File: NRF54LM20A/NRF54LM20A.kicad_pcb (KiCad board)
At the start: 4 copper layers, 10.8 x 22 mm, 39 parts, among them IC3 NMH1000T1, J1 Conn_ARM_SWD_TagConnect_TC203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, U1 S25HS512TFANHI010, U2 nRF54LM20A-QGAA, U3 SR4W035, U4 IM67D128BV01, U5 TXS0102DQE, Y1 CX2016DB32000D0WZRC1

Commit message: straight up routin it
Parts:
- added C25: 10u, Capacitor_SMD:C_0402_1005Metric, F.Cu at (89.5, 76.7)
- added C26: 10u, Capacitor_SMD:C_0603_1608Metric, F.Cu at (91.8, 81.0)
- added C27: 47n 25V, Capacitor_SMD:C_0402_1005Metric, F.Cu at (90.8, 82.7)
- added C28: 0.47u 25V, Capacitor_SMD:C_0402_1005Metric, F.Cu at (91.8, 82.7)
- added C29: 10n 25V, Capacitor_SMD:C_0201_0603Metric, F.Cu at (92.6, 82.8)
- added C30: 10u 16V, Capacitor_SMD:C_0603_1608Metric, F.Cu at (89.6, 82.2)
- added C31: 47n 25V, Capacitor_SMD:C_0402_1005Metric, F.Cu at (91.7, 89.0)
- added C32: 0.47u 25V, Capacitor_SMD:C_0402_1005Metric, F.Cu at (92.7, 89.0)
- added C33: 10n 25V, Capacitor_SMD:C_0201_0603Metric, F.Cu at (93.5, 88.8)
- added C34: TBD, Capacitor_SMD:C_0603_1608Metric, F.Cu at (91.7, 91.5)
- added C35: TBD, Capacitor_SMD:C_0603_1608Metric, F.Cu at (93.2, 91.5)
- added C36: TBD, Capacitor_SMD:C_0402_1005Metric, F.Cu at (90.5, 91.2)
- added C37: TBD, Capacitor_SMD:C_0402_1005Metric, F.Cu at (89.5, 91.2)
- added C38: 0.1u, Capacitor_SMD:C_0201_0603Metric, F.Cu at (93.9, 82.9)
- added C39: T527I107M006ATE070, Capacitor_Tantalum_SMD:CP_EIA-3216-12_Kemet-S, F.Cu at (89.8, 73.4)
- added C40: 0.1u, Capacitor_SMD:C_0201_0603Metric, F.Cu at (93.2, 79.5)
- added C41: 0.1u, Capacitor_SMD:C_0201_0603Metric, F.Cu at (91.4, 77.0)
- added C42: TBD, Capacitor_SMD:C_0201_0603Metric, F.Cu at (93.8, 77.2)
- added C43: TBD, Capacitor_SMD:C_0201_0603Metric, F.Cu at (93.5, 78.4)
- added IC1: TPS6285010MQDRLRQ1, Library:TPS6285010MQDRLRQ1, F.Cu at (91.6, 79.0)
- added IC2: BQ51013B, Package_DFN_QFN:Texas_VQFN-RHL-20_ThermalVias, F.Cu at (91.5, 85.8)
- added L2: 0.47u, Inductor_SMD:L_0603_1608Metric, F.Cu at (89.6, 79.2)
- added R1: 10k, Resistor_SMD:R_0201_0603Metric, F.Cu at (90.1, 88.8)
- added R2: TBD, Resistor_SMD:R_0201_0603Metric, F.Cu at (90.8, 88.8)
- added R3: TBD, Resistor_SMD:R_0201_0603Metric, F.Cu at (89.3, 88.8)
- added R4: TBD, Resistor_SMD:R_0201_0603Metric, F.Cu at (89.7, 90.0)
- added R5: 5.1k, Resistor_SMD:R_0201_0603Metric, F.Cu at (93.9, 80.0)
- added R6: 10k, Resistor_SMD:R_0201_0603Metric, F.Cu at (93.9, 81.5)
- added TP1: RCU-0C, digikey-footprints:PROBE_PAD_0603, B.Cu at (90.2, 92.0)
- added TP2: RCU-0C, digikey-footprints:PROBE_PAD_0603, B.Cu at (90.2, 90.5)
- added TP3: RCU-0C, digikey-footprints:PROBE_PAD_0603, B.Cu at (92.8, 90.5)
- added TP4: RCU-0C, digikey-footprints:PROBE_PAD_0603, B.Cu at (92.8, 92.0)
- added U6: LSM6DSV16B, Package_LGA:LGA-14_3x2.5mm_P0.5mm_LayoutBorder3x4y, F.Cu at (92.6, 74.5)
- C19: value 6TPS150MUD -> 10u; footprint Capacitor_Tantalum_SMD:CP_EIA-3528-21_Kemet-B -> Capacitor_SMD:C_0402_1005Metric
- moved C19 25.7 mm to (90.5, 76.7), turned to 90 degrees
- moved J1 19.8 mm to (92.5, 74.5), turned to 90 degrees
- moved C20 0.09 mm to (103.3, 76.6)
- moved C17 0.05 mm to (103.3, 73.7)
- moved C18 0.05 mm to (103.3, 75.2)
- moved U1 0.05 mm to (98.6, 74.3)
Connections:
- C19 pad 1: +5V -> +1V8
- C19 pad 2: unconnected-(C19-Pad2) -> GND
- U2 pad 13: unconnected-(U2C-P1.03-Pad13) -> /Peripherals/IMU_CS
- U2 pad 14: unconnected-(U2C-P1.04-Pad14) -> /Peripherals/IMU_INT0
- U2 pad 15: unconnected-(U2C-P1.05-Pad15) -> /Peripherals/5V_SENSE
- U2 pad 16: unconnected-(U2C-P1.06-Pad16) -> /Peripherals/5V_SENSE
- U2 pad 22: unconnected-(U2C-P1.07-Pad22) -> /Peripherals/IMU_SCK
- U2 pad 23: unconnected-(U2C-P1.08-Pad23) -> /Peripherals/IMU_INT1
- U2 pad 24: unconnected-(U2C-P1.09-Pad24) -> /Peripherals/IMU_SDI
- U2 pad 25: unconnected-(U2B-P0.03-Pad25) -> /Peripherals/IMU_SDO
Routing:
- net +5V: track 5.54 -> 36.3 mm, vias 2 -> 6
- net GND: track 33.1 -> 63.3 mm, vias 17 -> 25
- net /Peripherals/IMU_SDO: track 0.00 -> 20.8 mm, vias 0 -> 3
- net /Power/AC1: track 0.00 -> 19.7 mm, vias 0 -> 3
- net /SWCLK: track 0.50 -> 20.2 mm
- net /Peripherals/IMU_SDI: track 0.00 -> 19.6 mm, vias 0 -> 3
- net NFC2: track 1.26 -> 20.0 mm, vias 1 -> 3
- net /SWDIO: track 0.71 -> 19.2 mm
- net NFC1: track 1.09 -> 18.6 mm, vias 1 -> 3
- net /Peripherals/IMU_SCK: track 0.00 -> 16.6 mm, vias 0 -> 3
- net /~{RESET}: track 0.50 -> 15.8 mm
- net /Peripherals/IMU_INT1: track 0.00 -> 15.2 mm, vias 0 -> 3
- net /Power/AC2: track 0.00 -> 11.3 mm, vias 0 -> 6
- net Net-(IC2-RECT): track 0.00 -> 11.1 mm, vias 0 -> 3
- net +1V8: track 18.7 -> 28.9 mm, vias 10 -> 14
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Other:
- board size 10.8 x 22 mm -> 15 x 22 mm

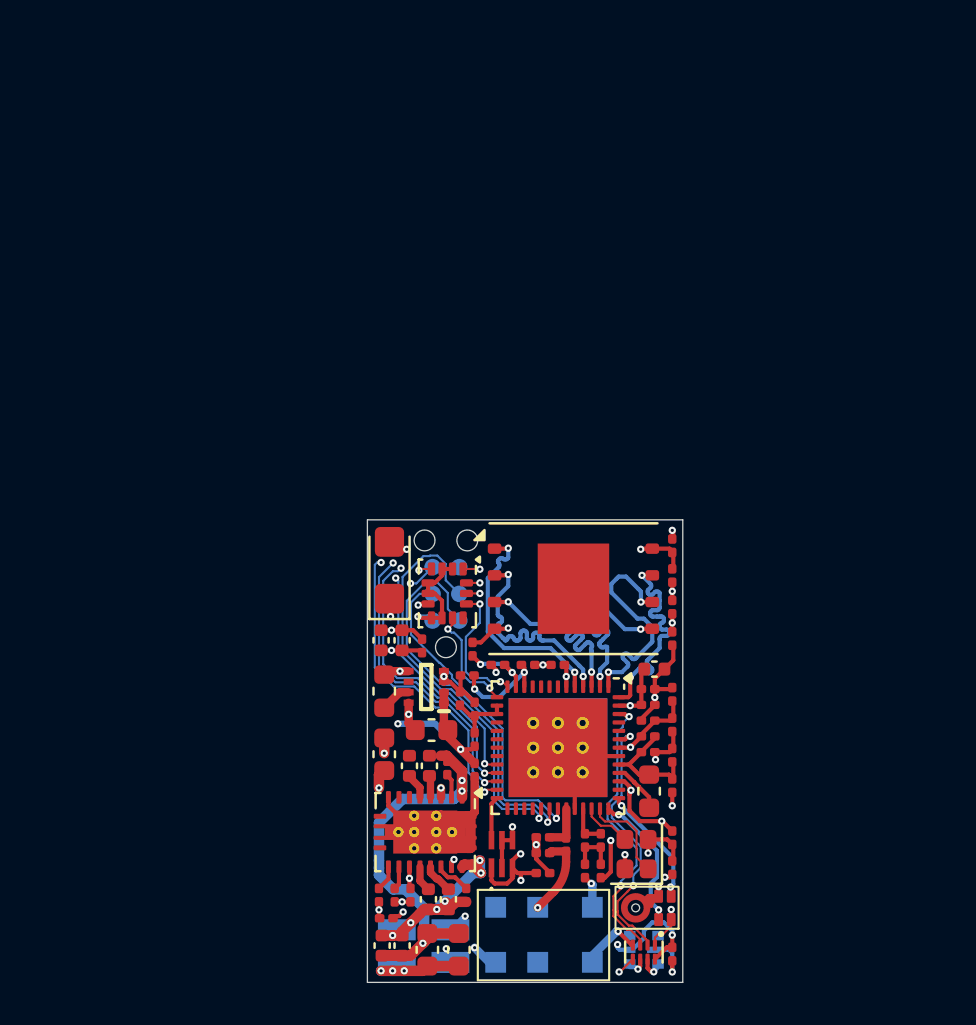
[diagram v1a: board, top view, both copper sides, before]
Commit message: switch to nrf54l15, antenna work
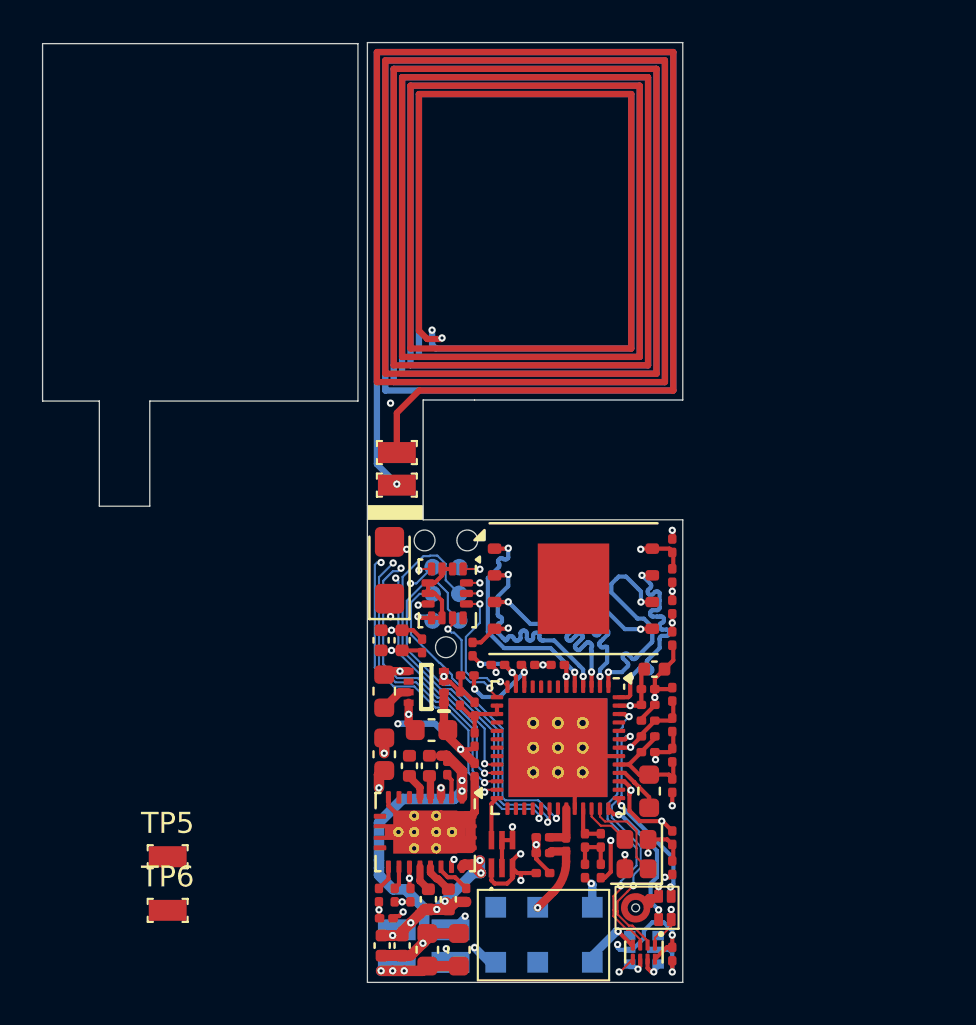
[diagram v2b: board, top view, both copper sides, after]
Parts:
- added TP5: RCU-0C, digikey-footprints:PROBE_PAD_0603, F.Cu at (79.3, 87.0)
- added TP6: RCU-0C, digikey-footprints:PROBE_PAD_0603, F.Cu at (79.3, 89.6)
- added TP7: RCU-0C, digikey-footprints:PROBE_PAD_0603, F.Cu at (90.2, 67.8)
- added TP8: RCU-0C, digikey-footprints:PROBE_PAD_0603, F.Cu at (90.2, 69.3)
- R5: value 5.1k -> 51k
- R6: value 10k -> 100k
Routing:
- net /QI-ANT: track 0.00 -> 1263.6 mm, vias 0 -> 4
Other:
- board size 15 x 22 mm -> 30.5 x 44.7 mm
